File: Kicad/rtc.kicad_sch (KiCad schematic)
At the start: 6 parts, among them Y901 32,768 Hz

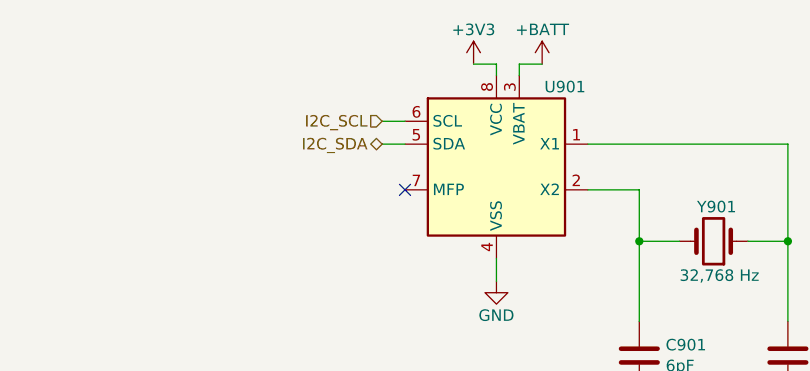
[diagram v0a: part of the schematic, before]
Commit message: Resolve DRC/ERC errors.
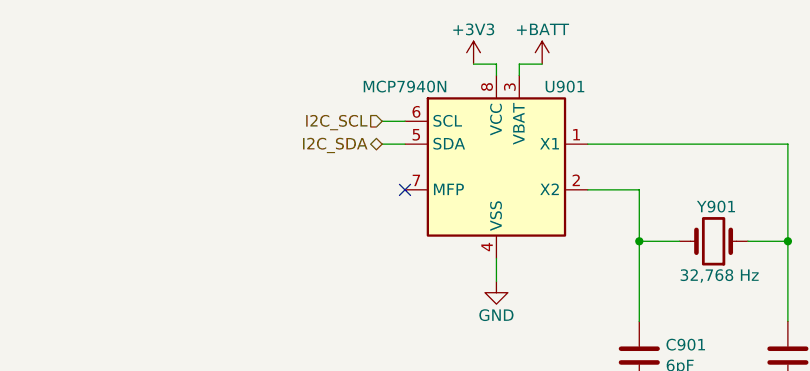
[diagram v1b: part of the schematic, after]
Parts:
- U901: value (none) -> MCP7940N; footprint (none) -> Package_DIP:DIP-8_W7.62mm
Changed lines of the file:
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@@
     (in_bom yes) (on_board yes)
     (property "Reference" "U901" (id 0) (at 111.125 59.055 0))
-    (property "Value" "" (id 1) (at 93.345 59.055 0))
-    (property "Footprint" "" (id 2) (at 103.505 67.945 0)
+    (property "Value" "MCP7940N" (id 1) (at 93.345 59.055 0))
+    (property "Footprint" "Package_DIP:DIP-8_W7.62mm" (id 2) (at 103.505 67.945 0)
       (effects (font (size 1.27 1.27)) hide)
     )
